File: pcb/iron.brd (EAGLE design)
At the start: 8 x 48 mm, 22 parts, among them IC1 AT24CS04-SOT23, IC2 TS507CLT, IC3 AD7995, IC4 ESDA6V1SC5, X1 LUMBERG_KLB_4

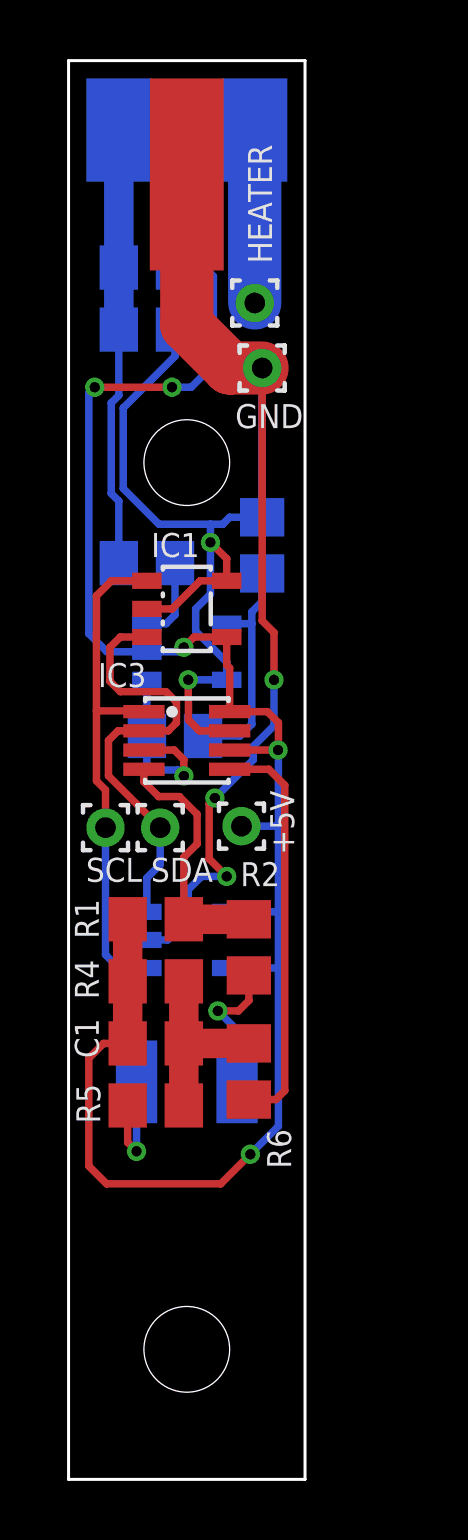
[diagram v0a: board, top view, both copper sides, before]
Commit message: reworked current path on boards and added new gerber files
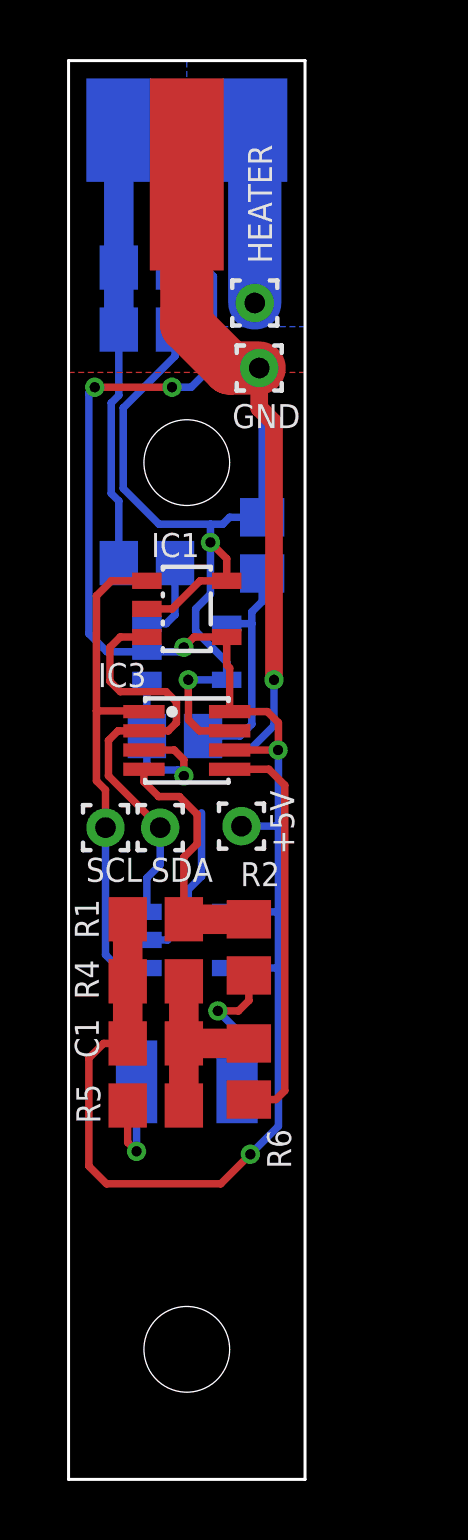
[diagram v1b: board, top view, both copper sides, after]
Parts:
- moved GND 0.10 mm to (6.45, 37.6)
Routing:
- net GND: track 66.8 -> 62.9 mm, vias 6 -> 4
- added copper zone on layer 1, net GND
- added copper zone on layer 16, net HEATER
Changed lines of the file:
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@@
 <grid distance="1" unitdist="mm" unit="mm" style="lines" multiple="1" display="no" altdistance="0.05" altunitdist="mm" altunit="mm"/>
 <layers>
-<layer number="1" name="Top" color="4" fill="1" visible="no" active="yes"/>
+<layer number="1" name="Top" color="4" fill="1" visible="yes" active="yes"/>
 <layer number="2" name="Route2" color="1" fill="3" visible="no" active="no"/>
 <layer number="3" name="Route3" color="4" fill="3" visible="no" active="no"/>
@@
 <layer number="14" name="Route14" color="1" fill="6" visible="no" active="no"/>
 <layer number="15" name="Route15" color="4" fill="6" visible="no" active="no"/>
-<layer number="16" name="Bottom" color="1" fill="1" visible="yes" active="yes"/>
+<layer number="16" name="Bottom" color="1" fill="1" visible="no" active="yes"/>
 <layer number="17" name="Pads" color="2" fill="1" visible="yes" active="yes"/>
 <layer number="18" name="Vias" color="2" fill="1" visible="yes" active="yes"/>
 <layer number="19" name="Unrouted" color="6" fill="1" visible="yes" active="yes"/>
 <layer number="20" name="Dimension" color="24" fill="1" visible="yes" active="yes"/>
-<layer number="21" name="tPlace" color="7" fill="1" visible="no" active="yes"/>
-<layer number="22" name="bPlace" color="7" fill="1" visible="yes" active="yes"/>
-<layer number="23" name="tOrigins" color="15" fill="1" visible="no" active="yes"/>
-<layer number="24" name="bOrigins" color="15" fill="1" visible="yes" active="yes"/>
+<layer number="21" name="tPlace" color="7" fill="1" visible="yes" active="yes"/>
+<layer number="22" name="bPlace" color="7" fill="1" visible="no" active="yes"/>
+<layer number="23" name="tOrigins" color="15" fill="1" visible="yes" active="yes"/>
+<layer number="24" name="bOrigins" color="15" fill="1" visible="no" active="yes"/>
 <layer number="25" name="tNames" color="7" fill="1" visible="no" active="yes"/>
 <layer number="26" name="bNames" color="7" fill="1" visible="no" active="yes"/>
@@
 <layer number="48" name="Document" color="7" fill="1" visible="no" active="yes"/>
 <layer number="49" name="Reference" color="7" fill="1" visible="no" active="yes"/>
-<layer number="51" name="tDocu" color="7" fill="1" visible="no" active="yes"/>
-<layer number="52" name="bDocu" color="7" fill="1" visible="yes" active="yes"/>
+<layer number="51" name="tDocu" color="7" fill="1" visible="yes" active="yes"/>
+<layer number="52" name="bDocu" color="7" fill="1" visible="no" active="yes"/>
 <layer number="88" name="SimResults" color="9" fill="1" visible="no" active="no"/>
 <layer number="89" name="SimProbes" color="9" fill="1" visible="no" active="no"/>
@@
 <attribute name="VALUE" x="6.3" y="40.4" size="0.0254" layer="27"/>
 </element>
-<element name="GND" library="solderpi" library_urn="urn:adsk.eagle:library:1437534" package="1,6/0,8" package3d_urn="urn:adsk.eagle:package:1581957/6" value="" x="6.55" y="37.6" smashed="yes">
-<attribute name="NAME" x="5.638" y="35.566" size="0.8128" layer="25" ratio="10"/>
-<attribute name="VALUE" x="6.55" y="38.2" size="0.0254" layer="27"/>
+<element name="GND" library="solderpi" library_urn="urn:adsk.eagle:library:1437534" package="1,6/0,8" package3d_urn="urn:adsk.eagle:package:1581957/6" value="" x="6.45" y="37.6" smashed="yes">
+<attribute name="NAME" x="5.538" y="35.566" size="0.8128" layer="25" ratio="10"/>
+<attribute name="VALUE" x="6.45" y="38.2" size="0.0254" layer="27"/>
 </element>
 <element name="SCL" library="solderpi" library_urn="urn:adsk.eagle:library:1437534" package="1,6/0,8" package3d_urn="urn:adsk.eagle:package:1581957/6" value="" x="1.25" y="22.05" smashed="yes">
@@
 <contactref element="C2" pad="2"/>
 <contactref element="GND" pad="1"/>
-<wire x1="6.55" y1="37.6" x2="6.55" y2="32.55" width="0.254" layer="16"/>
 <wire x1="6.55" y1="32.55" x2="5.4486375" y2="32.55" width="0.254" layer="16"/>
 <wire x1="4.8" y1="32.315" x2="3.0597375" y2="32.315" width="0.254" layer="16"/>
@@
 <wire x1="6.1" y1="16.2" x2="6.1" y2="17.05" width="0.254" layer="1"/>
 <wire x1="5.75" y1="15.85" x2="6.1" y2="16.2" width="0.254" layer="1"/>
-<via x="5.35" y="20.4" extent="1-16" drill="0.35"/>
-<wire x1="5.35" y1="20.4" x2="4.7564" y2="20.9936" width="0.254" layer="1"/>
-<wire x1="4.7564" y1="22.8564" x2="4.95" y2="23.05" width="0.254" layer="1"/>
-<via x="4.95" y="23.05" extent="1-16" drill="0.35"/>
-<wire x1="4.7564" y1="20.9936" x2="4.7564" y2="22.8564" width="0.254" layer="1"/>
-<wire x1="4.95" y1="23.05" x2="6.25" y2="24.35" width="0.254" layer="16"/>
-<wire x1="6.25" y1="24.35" x2="6.25" y2="24.8" width="0.254" layer="16"/>
 <wire x1="6.25" y1="24.8" x2="6.95" y2="25.5" width="0.254" layer="16"/>
 <wire x1="6.95" y1="25.5" x2="6.95" y2="27.05" width="0.254" layer="16"/>
 <via x="6.95" y="27.05" extent="1-16" drill="0.35"/>
-<wire x1="6.95" y1="27.05" x2="6.95" y2="28.65" width="0.254" layer="1"/>
-<wire x1="6.95" y1="28.65" x2="6.55" y2="29.05" width="0.254" layer="1"/>
-<wire x1="6.55" y1="29.05" x2="6.55" y2="37.6" width="0.254" layer="1"/>
-<wire x1="6.55" y1="37.6" x2="5.45" y2="37.6" width="1.8" layer="1"/>
+<wire x1="6.45" y1="37.6" x2="5.45" y2="37.6" width="1.8" layer="1"/>
 <wire x1="4" y1="39.05" x2="4" y2="44.15" width="1.8" layer="1"/>
 <wire x1="5.45" y1="37.6" x2="4" y2="39.05" width="1.8" layer="1"/>
@@
 <wire x1="3.5" y1="29.45" x2="4.45" y2="30.4" width="0.254" layer="1"/>
 <wire x1="4.45" y1="30.4" x2="5.35" y2="30.4" width="0.254" layer="1"/>
-<polygon width="0.2" layer="16" isolate="0.3048">
+<polygon width="0.2" layer="16" isolate="0.3048" rank="2">
 <vertex x="0" y="48"/>
 <vertex x="8" y="48"/>
@@
 <wire x1="3.35" y1="18.25" x2="4.05" y2="18.95" width="0.254" layer="16"/>
 <wire x1="4.05" y1="18.95" x2="4.05" y2="19.95" width="0.254" layer="16"/>
-<wire x1="4.5" y1="20.4" x2="5.35" y2="20.4" width="0.254" layer="16"/>
 <wire x1="4.05" y1="19.95" x2="4.5" y2="20.4" width="0.254" layer="16"/>
+<polygon width="0.2" layer="1" isolate="0.3048" thermals="no">
+<vertex x="0" y="48"/>
+<vertex x="8" y="48"/>
+<vertex x="8" y="37.45"/>
+<vertex x="0" y="37.45"/>
+</polygon>
+<wire x1="6.95" y1="27.05" x2="6.95" y2="35.75" width="0.6" layer="1"/>
+<wire x1="4.5" y1="20.4" x2="4.5" y2="22.55" width="0.254" layer="16"/>
+<wire x1="6.45" y1="37.6" x2="6.55" y2="37.5" width="0.254" layer="16"/>
+<wire x1="6.55" y1="37.5" x2="6.55" y2="36" width="0.254" layer="16"/>
+<wire x1="6.55" y1="36" x2="6.55" y2="32.55" width="0.254" layer="16"/>
+<wire x1="6.45" y1="36.25" x2="6.45" y2="37.6" width="0.6" layer="1"/>
+<wire x1="6.95" y1="35.75" x2="6.45" y2="36.25" width="0.6" layer="1"/>
 </signal>
 <signal name="AD_COMP">
@@
 <wire x1="4.25" y1="28.5" x2="5.35" y2="28.5" width="0.254" layer="1"/>
 <wire x1="5.35" y1="27.55" x2="5.35" y2="28.5" width="0.254" layer="1"/>
-<polygon width="0.1524" layer="1" isolate="0.3048">
+<polygon width="0.1524" layer="1" isolate="0.3048" rank="2">
 <vertex x="0" y="48"/>
 <vertex x="8" y="48"/>
@@
 <contactref element="HEATER" pad="1"/>
 <wire x1="6.3" y1="45.65" x2="6.3" y2="39.8" width="1.8" layer="16"/>
+<polygon width="0.2" layer="16" isolate="0.3048" thermals="no">
+<vertex x="4" y="48"/>
+<vertex x="8" y="48"/>
+<vertex x="8" y="39"/>
+<vertex x="5" y="39"/>
+<vertex x="4" y="39"/>
+</polygon>
 </signal>
 </signals>

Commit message: fixed vcc,vdd on opAmp
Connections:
- net +5V: now also IC2.5; no longer IC2.2
- net GND: now also IC2.2; no longer IC2.5
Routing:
- net +5V: track 63.6 -> 57.1 mm, vias 5 -> 4
- net GND: track 62.9 -> 60.1 mm
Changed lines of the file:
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@@
 <?xml version="1.0" encoding="utf-8"?>
 <!DOCTYPE eagle SYSTEM "eagle.dtd">
-<eagle version="9.0.0">
+<eagle version="9.0.1">
 <drawing>
 <settings>
@@
 <grid distance="1" unitdist="mm" unit="mm" style="lines" multiple="1" display="no" altdistance="0.05" altunitdist="mm" altunit="mm"/>
 <layers>
-<layer number="1" name="Top" color="4" fill="1" visible="yes" active="yes"/>
+<layer number="1" name="Top" color="4" fill="1" visible="no" active="yes"/>
 <layer number="2" name="Route2" color="1" fill="3" visible="no" active="no"/>
 <layer number="3" name="Route3" color="4" fill="3" visible="no" active="no"/>
@@
 <layer number="14" name="Route14" color="1" fill="6" visible="no" active="no"/>
 <layer number="15" name="Route15" color="4" fill="6" visible="no" active="no"/>
-<layer number="16" name="Bottom" color="1" fill="1" visible="no" active="yes"/>
+<layer number="16" name="Bottom" color="1" fill="1" visible="yes" active="yes"/>
 <layer number="17" name="Pads" color="2" fill="1" visible="yes" active="yes"/>
 <layer number="18" name="Vias" color="2" fill="1" visible="yes" active="yes"/>
 <layer number="19" name="Unrouted" color="6" fill="1" visible="yes" active="yes"/>
 <layer number="20" name="Dimension" color="24" fill="1" visible="yes" active="yes"/>
-<layer number="21" name="tPlace" color="7" fill="1" visible="yes" active="yes"/>
-<layer number="22" name="bPlace" color="7" fill="1" visible="no" active="yes"/>
-<layer number="23" name="tOrigins" color="15" fill="1" visible="yes" active="yes"/>
-<layer number="24" name="bOrigins" color="15" fill="1" visible="no" active="yes"/>
+<layer number="21" name="tPlace" color="7" fill="1" visible="no" active="yes"/>
+<layer number="22" name="bPlace" color="7" fill="1" visible="yes" active="yes"/>
+<layer number="23" name="tOrigins" color="15" fill="1" visible="no" active="yes"/>
+<layer number="24" name="bOrigins" color="15" fill="1" visible="yes" active="yes"/>
 <layer number="25" name="tNames" color="7" fill="1" visible="no" active="yes"/>
 <layer number="26" name="bNames" color="7" fill="1" visible="no" active="yes"/>
@@
 <layer number="48" name="Document" color="7" fill="1" visible="no" active="yes"/>
 <layer number="49" name="Reference" color="7" fill="1" visible="no" active="yes"/>
-<layer number="51" name="tDocu" color="7" fill="1" visible="yes" active="yes"/>
-<layer number="52" name="bDocu" color="7" fill="1" visible="no" active="yes"/>
+<layer number="51" name="tDocu" color="7" fill="1" visible="no" active="yes"/>
+<layer number="52" name="bDocu" color="7" fill="1" visible="yes" active="yes"/>
 <layer number="88" name="SimResults" color="9" fill="1" visible="no" active="no"/>
 <layer number="89" name="SimProbes" color="9" fill="1" visible="no" active="no"/>
@@
 <contactref element="R3" pad="P$1"/>
 <contactref element="R10" pad="1"/>
-<contactref element="IC2" pad="5"/>
 <contactref element="C2" pad="2"/>
 <contactref element="GND" pad="1"/>
 <wire x1="6.55" y1="32.55" x2="5.4486375" y2="32.55" width="0.254" layer="16"/>
 <wire x1="4.8" y1="32.315" x2="3.0597375" y2="32.315" width="0.254" layer="16"/>
-<wire x1="4.8" y1="29.95" x2="4.3" y2="29.45" width="0.254" layer="16"/>
 <wire x1="4.8" y1="29.95" x2="4.8" y2="31.7" width="0.254" layer="16"/>
 <wire x1="4.8" y1="31.7" x2="4.8" y2="32.315" width="0.254" layer="16"/>
@@
 <wire x1="4.0564" y1="26.4683375" x2="4.0564" y2="25.6936" width="0.254" layer="1"/>
 <wire x1="4.425" y1="25.325" x2="5.45" y2="25.325" width="0.254" layer="1"/>
-<wire x1="5.35" y1="27.05" x2="4.05" y2="27.05" width="0.254" layer="16"/>
 <wire x1="4.0564" y1="25.6936" x2="4.425" y2="25.325" width="0.254" layer="1"/>
-<wire x1="4.3" y1="29.45" x2="4.3" y2="28.7" width="0.254" layer="16"/>
-<wire x1="4.3" y1="28.7" x2="5.35" y2="27.65" width="0.254" layer="16"/>
-<wire x1="5.35" y1="27.65" x2="5.35" y2="27.05" width="0.254" layer="16"/>
 <wire x1="5.7" y1="15.2" x2="5.05" y2="15.85" width="0.254" layer="16"/>
 <via x="5.05" y="15.85" extent="1-16" drill="0.35"/>
@@
 <wire x1="6.1" y1="16.2" x2="6.1" y2="17.05" width="0.254" layer="1"/>
 <wire x1="5.75" y1="15.85" x2="6.1" y2="16.2" width="0.254" layer="1"/>
-<wire x1="6.25" y1="24.8" x2="6.95" y2="25.5" width="0.254" layer="16"/>
-<wire x1="6.95" y1="25.5" x2="6.95" y2="27.05" width="0.254" layer="16"/>
 <via x="6.95" y="27.05" extent="1-16" drill="0.35"/>
 <wire x1="6.45" y1="37.6" x2="5.45" y2="37.6" width="1.8" layer="1"/>
@@
 <wire x1="4.5" y1="20.4" x2="4.5" y2="22.55" width="0.254" layer="16"/>
 <wire x1="6.45" y1="37.6" x2="6.55" y2="37.5" width="0.254" layer="16"/>
-<wire x1="6.55" y1="37.5" x2="6.55" y2="36" width="0.254" layer="16"/>
-<wire x1="6.55" y1="36" x2="6.55" y2="32.55" width="0.254" layer="16"/>
+<wire x1="6.55" y1="37.5" x2="6.55" y2="32.55" width="0.254" layer="16"/>
 <wire x1="6.45" y1="36.25" x2="6.45" y2="37.6" width="0.6" layer="1"/>
 <wire x1="6.95" y1="35.75" x2="6.45" y2="36.25" width="0.6" layer="1"/>
+<contactref element="IC2" pad="2"/>
+<wire x1="4.05" y1="27.05" x2="4.05" y2="28" width="0.254" layer="16"/>
+<wire x1="4.05" y1="28" x2="4.05" y2="29.2" width="0.254" layer="16"/>
+<wire x1="4.05" y1="29.2" x2="4.8" y2="29.95" width="0.254" layer="16"/>
+<wire x1="2.65" y1="28" x2="4.05" y2="28" width="0.254" layer="16"/>
 </signal>
 <signal name="AD_COMP">
@@
 <contactref element="IC3" pad="6"/>
 <contactref element="R9" pad="2"/>
-<contactref element="IC2" pad="2"/>
 <contactref element="+5V" pad="1"/>
 <wire x1="3.6" y1="41" x2="4.6" y2="41" width="0.254" layer="16"/>
-<wire x1="4.6" y1="41" x2="4.9" y2="40.7" width="0.254" layer="16"/>
-<wire x1="4.9" y1="40.7" x2="4.9" y2="37.7" width="0.254" layer="16"/>
-<wire x1="4.15" y1="36.95" x2="3.5" y2="36.95" width="0.254" layer="16"/>
-<via x="3.5" y="36.95" extent="1-16" drill="0.35"/>
-<wire x1="4.9" y1="37.7" x2="4.15" y2="36.95" width="0.254" layer="16"/>
-<wire x1="5.45" y1="25.975" x2="5.45" y2="27.45" width="0.254" layer="1"/>
-<wire x1="5.45" y1="27.45" x2="5.35" y2="27.55" width="0.254" layer="1"/>
-<wire x1="0.6858" y1="28.6142" x2="1.3" y2="28" width="0.254" layer="16"/>
-<wire x1="1.3" y1="28" x2="2.65" y2="28" width="0.254" layer="16"/>
-<via x="0.8862" y="36.95" extent="1-16" drill="0.35"/>
-<wire x1="0.8862" y1="36.95" x2="0.6858" y2="36.7496" width="0.254" layer="16"/>
-<wire x1="3.5" y1="36.95" x2="0.8862" y2="36.95" width="0.254" layer="1"/>
-<wire x1="0.6858" y1="36.7496" x2="0.6858" y2="28.6142" width="0.254" layer="16"/>
+<wire x1="4.9" y1="40.7" x2="4.6" y2="41" width="0.254" layer="16"/>
 <via x="7.0892" y="24.675" extent="1-16" drill="0.35"/>
 <wire x1="5.45" y1="24.675" x2="7.0892" y2="24.675" width="0.254" layer="1"/>
@@
 <wire x1="7.1" y1="25.6" x2="7.1" y2="24.6858" width="0.254" layer="1"/>
 <wire x1="7.1" y1="24.6858" x2="7.0892" y2="24.675" width="0.254" layer="1"/>
-<wire x1="2.65" y1="28" x2="3.75" y2="28" width="0.254" layer="16"/>
-<wire x1="3.75" y1="28" x2="3.9" y2="28.15" width="0.254" layer="16"/>
-<via x="3.9" y="28.15" extent="1-16" drill="0.35"/>
-<wire x1="3.9" y1="28.15" x2="4.25" y2="28.5" width="0.254" layer="1"/>
 <contactref element="IC1" pad="4"/>
-<wire x1="4.25" y1="28.5" x2="5.35" y2="28.5" width="0.254" layer="1"/>
-<wire x1="5.35" y1="27.55" x2="5.35" y2="28.5" width="0.254" layer="1"/>
 <polygon width="0.1524" layer="1" isolate="0.3048" rank="2">
 <vertex x="0" y="48"/>
@@
 <wire x1="5.35" y1="17.3" x2="7.1" y2="17.3" width="0.254" layer="16"/>
 <wire x1="5.85" y1="22.1" x2="7.1" y2="22.1" width="0.254" layer="16"/>
+<contactref element="IC2" pad="5"/>
+<wire x1="5.35" y1="27.05" x2="5.35" y2="27.75" width="0.254" layer="16"/>
+<via x="5.35" y="27.75" extent="1-16" drill="0.35"/>
+<wire x1="5.35" y1="27.75" x2="5.35" y2="28.5" width="0.254" layer="1"/>
+<wire x1="5.45" y1="25.975" x2="5.35" y2="25.975" width="0.254" layer="1"/>
+<wire x1="5.35" y1="25.975" x2="5.35" y2="27.75" width="0.254" layer="1"/>
+<wire x1="5.35" y1="28.5" x2="6.1" y2="28.5" width="0.254" layer="1"/>
+<wire x1="6.1" y1="28.5" x2="6.3" y2="28.7" width="0.254" layer="1"/>
+<wire x1="6.3" y1="28.7" x2="6.3" y2="35.4" width="0.254" layer="1"/>
+<wire x1="6.3" y1="35.4" x2="5.6" y2="36.1" width="0.254" layer="1"/>
+<via x="5.6" y="36.1" extent="1-16" drill="0.35"/>
+<wire x1="5.6" y1="36.1" x2="4.9" y2="36.8" width="0.254" layer="16"/>
+<wire x1="4.9" y1="36.8" x2="4.9" y2="40.7" width="0.254" layer="16"/>
 </signal>
 <signal name="SCL">
